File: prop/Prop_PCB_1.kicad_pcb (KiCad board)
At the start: 4 copper layers, 63.5 x 63.5 mm, 16 parts, among them J1 1984989, J2 1984989, J3 1984989, J4 1984989, J5 CAS_stacking, J6 Conn_01x02, J7 1984989, U1 L298P, U1301 MAX6675ISA+, U2 SN74LVC8T245DBR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

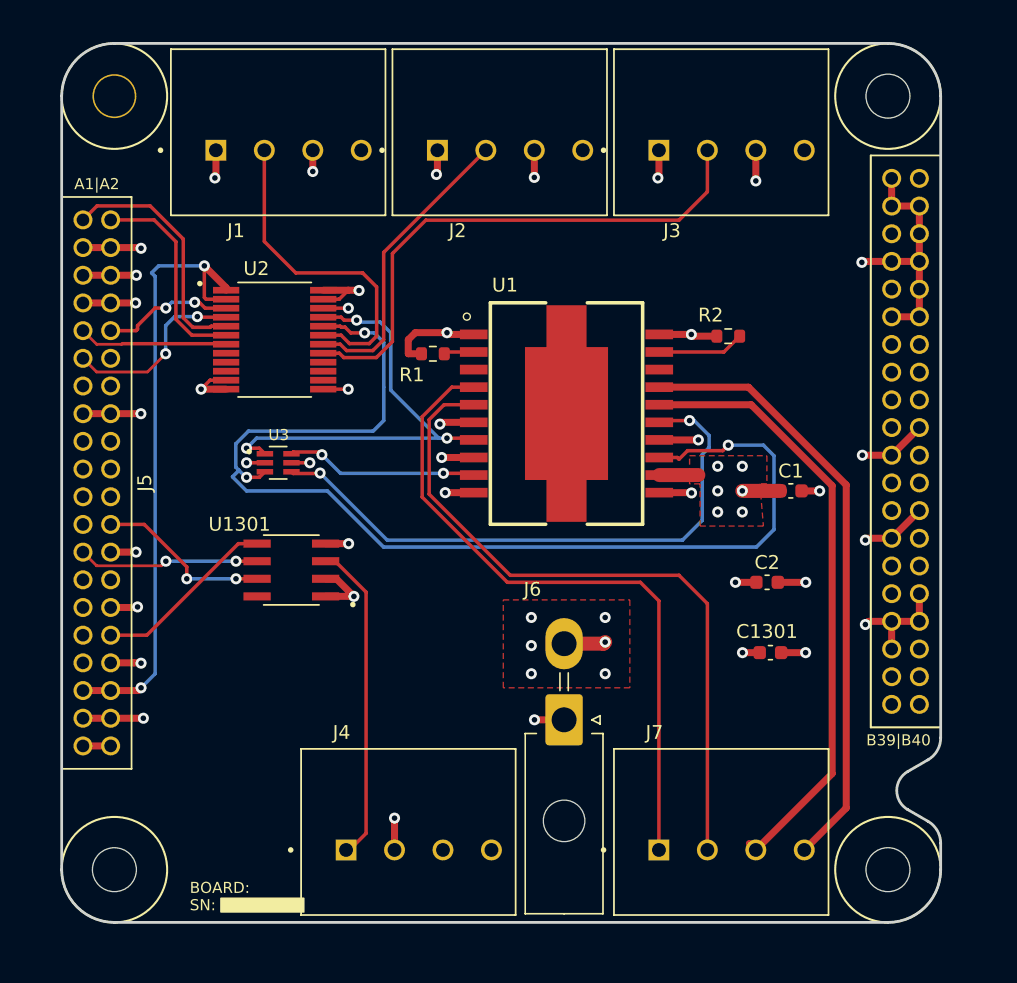
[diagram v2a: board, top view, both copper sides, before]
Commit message: Set minimum clearance to 0.25 mm.
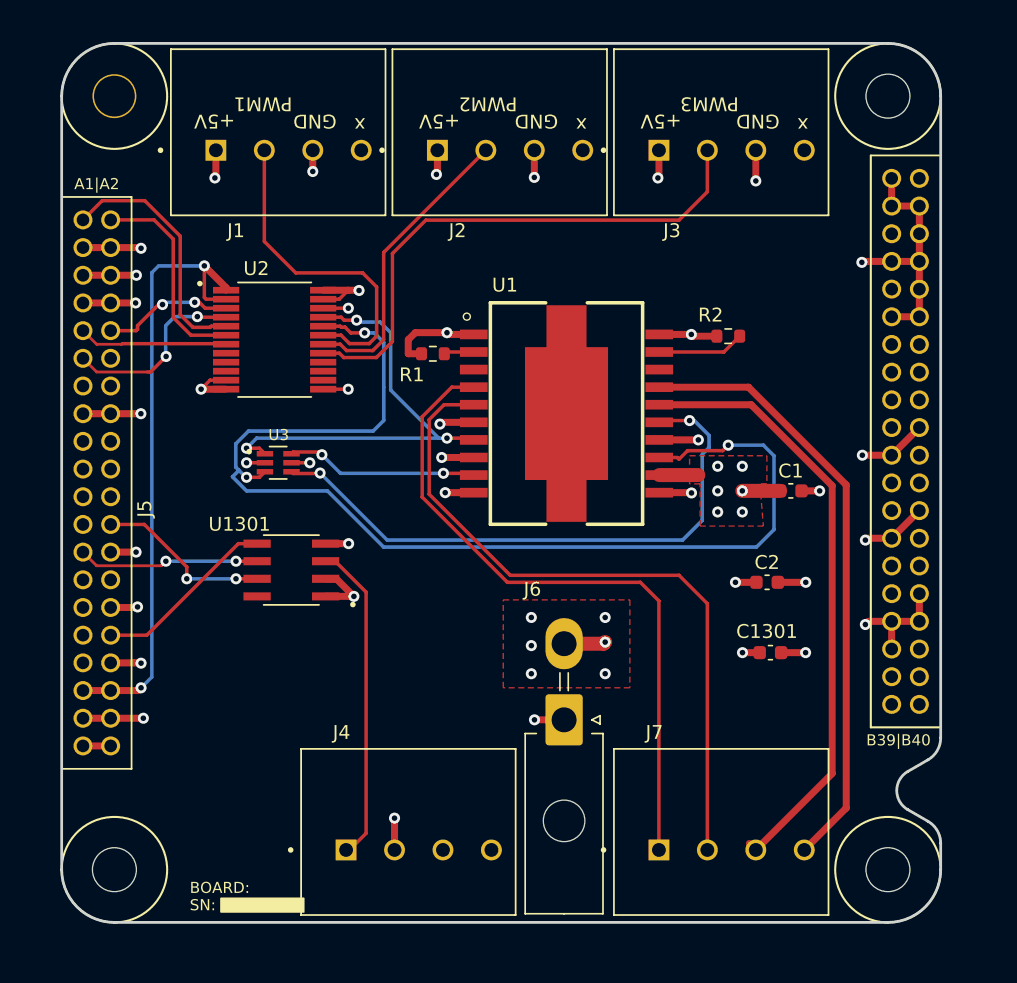
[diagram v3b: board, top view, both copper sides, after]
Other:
- board text added: "+5V"
- board text added: "GND"
- board text added: "PWM1"
- board text added: "PWM2"
- board text added: "PWM3"
- board text added: "x"
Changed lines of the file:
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@@
     (property "Sheetname" "CAS_bus")
     (attr through_hole)
-    (fp_text reference "J5" (at 6 31.75 90) (layer "F.SilkS")
+    (fp_text reference "J5" (at 6 33.615 90) (layer "F.SilkS")
       (effects (font (size 1 1) (thickness 0.15)))
     )
@@
       (effects (font (size 0.8 0.8) (thickness 0.15)))
     )
-    (fp_text user "ESQT-120-XX-XX-D" (at 57.277 35.767 270) (layer "F.Fab")
-      (effects (font (size 1 1) (thickness 0.015)))
-    )
-    (fp_text user "ESQT-120-XX-XX-D" (at 6.223 24.558 90) (layer "F.Fab")
+    (fp_text user "ESQT-120-XX-XX-D" (at 56.795 17.615 270) (layer "F.Fab")
       (effects (font (size 1 1) (thickness 0.015)))
     )
@@
     (pad "4" thru_hole circle locked (at 6 1.3) (size 1.508 1.508) (drill 1) (layers *.Cu *.Mask)
       (net 37 "unconnected-(J2-Pad4)") (pinfunction "4") (pintype "passive+no_connect"))
+  )
+  (gr_text "+5V" (at 97.25 50.25 180) (layer "F.SilkS")
+    (effects (font (size 1 1) (thickness 0.15)))
+  )
+  (gr_text "x" (at 91.5 50.5 180) (layer "F.SilkS")
+    (effects (font (size 1 1) (thickness 0.15)))
+  )
+  (gr_text "x" (at 107.5 50.5 180) (layer "F.SilkS")
+    (effects (font (size 1 1) (thickness 0.15)))
+  )
+  (gr_text "+5V" (at 81.25 50.25 180) (layer "F.SilkS")
+    (effects (font (size 1 1) (thickness 0.15)))
+  )
+  (gr_text "x" (at 75.5 50.5 180) (layer "F.SilkS")
+    (effects (font (size 1 1) (thickness 0.15)))
+  )
+  (gr_text "PWM2" (at 84.75 49 180) (layer "F.SilkS")
+    (effects (font (size 1 1) (thickness 0.15)))
+  )
+  (gr_text "+5V" (at 65 50.25 180) (layer "F.SilkS")
+    (effects (font (size 1 1) (thickness 0.15)))
+  )
+  (gr_text "GND" (at 88.25 50.25 180) (layer "F.SilkS")
+    (effects (font (size 1 1) (thickness 0.15)))
+  )
+  (gr_text "PWM3" (at 100.75 49 180) (layer "F.SilkS")
+    (effects (font (size 1 1) (thickness 0.15)))
+  )
+  (gr_text "GND" (at 104.25 50.25 180) (layer "F.SilkS")
+    (effects (font (size 1 1) (thickness 0.15)))
+  )
+  (gr_text "PWM1" (at 68.5 49 180) (layer "F.SilkS")
+    (effects (font (size 1 1) (thickness 0.15)))
+  )
+  (gr_text "GND" (at 72.25 50.25 180) (layer "F.SilkS")
+    (effects (font (size 1 1) (thickness 0.15)))
   )
   (segment (start 113.915 56.3851) (end 115.915 56.3851) (width 0.508) (layer "F.Cu") (net 1))
@@
   (via (at 64.262 60.706) (size 0.8) (drill 0.4) (layers "F.Cu" "B.Cu") (net 21))
   (via (at 59.69 91.186) (size 0.8) (drill 0.4) (layers "F.Cu" "B.Cu") (net 21))
-  (segment (start 60.706 61.468) (end 60.706 90.17) (width 0.254) (layer "B.Cu") (net 21))
-  (segment (start 60.706 90.17) (end 59.69 91.186) (width 0.254) (layer "B.Cu") (net 21))
-  (segment (start 60.96 60.706) (end 60.452 61.214) (width 0.254) (layer "B.Cu") (net 21))
-  (segment (start 60.452 61.214) (end 60.706 61.468) (width 0.254) (layer "B.Cu") (net 21))
+  (segment (start 60.464511 61.201489) (end 60.96 60.706) (width 0.25) (layer "B.Cu") (net 21))
+  (segment (start 59.69 91.186) (end 60.464511 90.411489) (width 0.25) (layer "B.Cu") (net 21))
+  (segment (start 60.464511 90.411489) (end 60.464511 61.201489) (width 0.25) (layer "B.Cu") (net 21))
   (segment (start 64.262 60.706) (end 60.96 60.706) (width 0.254) (layer "B.Cu") (net 21))
   (segment (start 64.322916 63.765) (end 63.905958 63.348042) (width 0.254) (layer "F.Cu") (net 22))
+  (segment (start 60.96 63.5) (end 60.706 63.754) (width 0.25) (layer "F.Cu") (net 22))
   (segment (start 59.436 65.278) (end 59.329 65.385) (width 0.254) (layer "F.Cu") (net 22))
   (segment (start 60.706 63.754) (end 59.436 65.024) (width 0.254) (layer "F.Cu") (net 22))
   (segment (start 63.905958 63.348042) (end 63.897177 63.339261) (width 0.254) (layer "F.Cu") (net 22))
-  (segment (start 61.4825 63.754) (end 60.706 63.754) (width 0.254) (layer "F.Cu") (net 22))
   (segment (start 59.436 65.024) (end 59.436 65.278) (width 0.254) (layer "F.Cu") (net 22))
   (segment (start 63.897177 63.339261) (end 63.567477 63.339261) (width 0.254) (layer "F.Cu") (net 22))
@@
   (segment (start 65.837 63.765) (end 65.833489 63.768511) (width 0.254) (layer "F.Cu") (net 22))
   (segment (start 59.329 65.385) (end 57.495 65.385) (width 0.254) (layer "F.Cu") (net 22))
+  (segment (start 61.239011 63.5) (end 60.96 63.5) (width 0.25) (layer "F.Cu") (net 22))
+  (via (at 61.239011 63.5) (size 0.8) (drill 0.4) (layers "F.Cu" "B.Cu") (net 22))
   (via (at 63.567477 63.339261) (size 0.8) (drill 0.4) (layers "F.Cu" "B.Cu") (net 22))
-  (via (at 61.4825 63.754) (size 0.8) (drill 0.4) (layers "F.Cu" "B.Cu") (net 22))
+  (segment (start 61.39975 63.339261) (end 61.239011 63.5) (width 0.25) (layer "B.Cu") (net 22))
   (segment (start 63.567477 63.339261) (end 61.897239 63.339261) (width 0.254) (layer "B.Cu") (net 22))
-  (segment (start 61.897239 63.339261) (end 61.4825 63.754) (width 0.254) (layer "B.Cu") (net 22))
+  (segment (start 61.897239 63.339261) (end 61.39975 63.339261) (width 0.25) (layer "B.Cu") (net 22))
+  (segment (start 60.378089 68.371911) (end 60.152089 68.371911) (width 0.254) (layer "F.Cu") (net 23))
   (segment (start 65.837 64.415) (end 65.803511 64.381511) (width 0.254) (layer "F.Cu") (net 23))
-  (segment (start 61.468 67.056) (end 60.152089 68.371911) (width 0.2032) (layer "F.Cu") (net 23))
+  (segment (start 61.5 67.25) (end 60.378089 68.371911) (width 0.254) (layer "F.Cu") (net 23))
   (segment (start 63.798841 64.415) (end 63.755605 64.371764) (width 0.254) (layer "F.Cu") (net 23))
   (segment (start 65.837 64.415) (end 63.798841 64.415) (width 0.254) (layer "F.Cu") (net 23))
   (segment (start 56.481911 68.371911) (end 55.495 67.385) (width 0.2032) (layer "F.Cu") (net 23))
   (segment (start 60.152089 68.371911) (end 56.481911 68.371911) (width 0.2032) (layer "F.Cu") (net 23))
+  (via (at 61.5 67.25) (size 0.8) (drill 0.4) (layers "F.Cu" "B.Cu") (net 23))
   (via (at 63.755605 64.371764) (size 0.8) (drill 0.4) (layers "F.Cu" "B.Cu") (net 23))
-  (via (at 61.468 67.056) (size 0.8) (drill 0.4) (layers "F.Cu" "B.Cu") (net 23))
   (segment (start 62.120236 64.371764) (end 61.468 65.024) (width 0.254) (layer "B.Cu") (net 23))
+  (segment (start 61.468 65.024) (end 61.468 67.218) (width 0.25) (layer "B.Cu") (net 23))
+  (segment (start 61.468 67.218) (end 61.5 67.25) (width 0.25) (layer "B.Cu") (net 23))
   (segment (start 63.755605 64.371764) (end 62.120236 64.371764) (width 0.254) (layer "B.Cu") (net 23))
-  (segment (start 61.468 65.024) (end 61.468 67.056) (width 0.254) (layer "B.Cu") (net 23))
   (segment (start 65.837 65.065) (end 64.763557 65.065) (width 0.254) (layer "F.Cu") (net 24))
+  (segment (start 62.519041 58.556957) (end 59.962084 56) (width 0.254) (layer "F.Cu") (net 24))
   (segment (start 64.763557 65.065) (end 64.680282 65.148275) (width 0.254) (layer "F.Cu") (net 24))
-  (segment (start 62.738 58.762) (end 60.348689 56.372689) (width 0.254) (layer "F.Cu") (net 24))
-  (segment (start 60.348689 56.372689) (end 56.507311 56.372689) (width 0.254) (layer "F.Cu") (net 24))
-  (segment (start 56.507311 56.372689) (end 55.495 57.385) (width 0.254) (layer "F.Cu") (net 24))
+  (segment (start 56.88 56) (end 55.495 57.385) (width 0.254) (layer "F.Cu") (net 24))
+  (segment (start 62.519042 64.233354) (end 62.519041 58.556957) (width 0.254) (layer "F.Cu") (net 24))
   (segment (start 64.680282 65.148275) (end 63.433963 65.148275) (width 0.254) (layer "F.Cu") (net 24))
-  (segment (start 63.433963 65.148275) (end 62.738 64.452312) (width 0.254) (layer "F.Cu") (net 24))
-  (segment (start 62.738 64.452312) (end 62.738 58.762) (width 0.254) (layer "F.Cu") (net 24))
+  (segment (start 59.962084 56) (end 56.88 56) (width 0.254) (layer "F.Cu") (net 24))
+  (segment (start 63.433963 65.148275) (end 62.519042 64.233354) (width 0.254) (layer "F.Cu") (net 24))
+  (segment (start 65.837 65.715) (end 63.288604 65.715) (width 0.254) (layer "F.Cu") (net 25))
+  (segment (start 62.015522 58.765522) (end 60.635 57.385) (width 0.254) (layer "F.Cu") (net 25))
   (segment (start 60.635 57.385) (end 57.495 57.385) (width 0.254) (layer "F.Cu") (net 25))
-  (segment (start 65.837 65.715) (end 63.359314 65.715) (width 0.254) (layer "F.Cu") (net 25))
-  (segment (start 62.209011 64.564697) (end 62.209011 58.959011) (width 0.254) (layer "F.Cu") (net 25))
-  (segment (start 62.209011 58.959011) (end 60.635 57.385) (width 0.254) (layer "F.Cu") (net 25))
-  (segment (start 63.359314 65.715) (end 62.209011 64.564697) (width 0.254) (layer "F.Cu") (net 25))
+  (segment (start 63.288604 65.715) (end 62.015522 64.441918) (width 0.254) (layer "F.Cu") (net 25))
+  (segment (start 62.015522 64.441918) (end 62.015522 58.765522) (width 0.254) (layer "F.Cu") (net 25))
   (segment (start 65.801489 66.329489) (end 58.329489 66.329489) (width 0.254) (layer "F.Cu") (net 26))
   (segment (start 58.329489 66.329489) (end 58.287067 66.371911) (width 0.2032) (layer "F.Cu") (net 26))
   (segment (start 56.481911 66.371911) (end 55.495 65.385) (width 0.2032) (layer "F.Cu") (net 26))
-  (segment (start 65.837 66.365) (end 65.801489 66.329489) (width 0.254) (layer "F.Cu") (net 26))
   (segment (start 58.287067 66.371911) (end 56.481911 66.371911) (width 0.2032) (layer "F.Cu") (net 26))
   (segment (start 77.849042 66.168958) (end 77.849042 59.815042) (width 0.254) (layer "F.Cu") (net 33))

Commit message: Updated hard-sch-blocks
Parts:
- moved C1301 24.7 mm to (80.5, 89.2)
- moved C2 24.7 mm to (80.3, 84.2)
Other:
- board text added: "Lead1"
- board text added: "Lead2"
- board text added: "Sol1"
- board text added: "Sol2"
- board text added: "T+"

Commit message: Added Star, BAC logo.
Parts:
- added Ref**: Val**, star-common-lib:star_fancy, F.Cu at (66.0, 91.0)
- added Ref**: Val**, star-common-lib:bac, F.Cu at (66.5, 98.8)

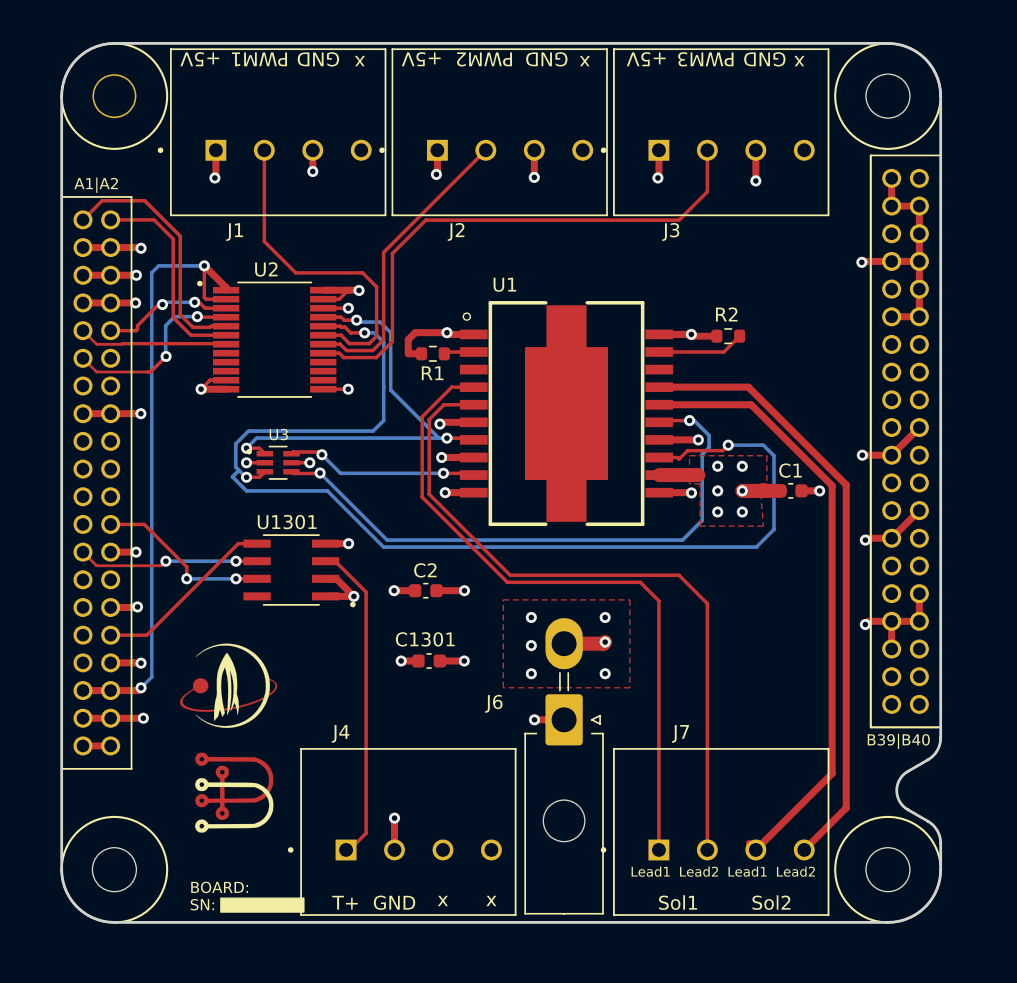
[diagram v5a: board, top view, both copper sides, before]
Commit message: Added front/back ground pour.
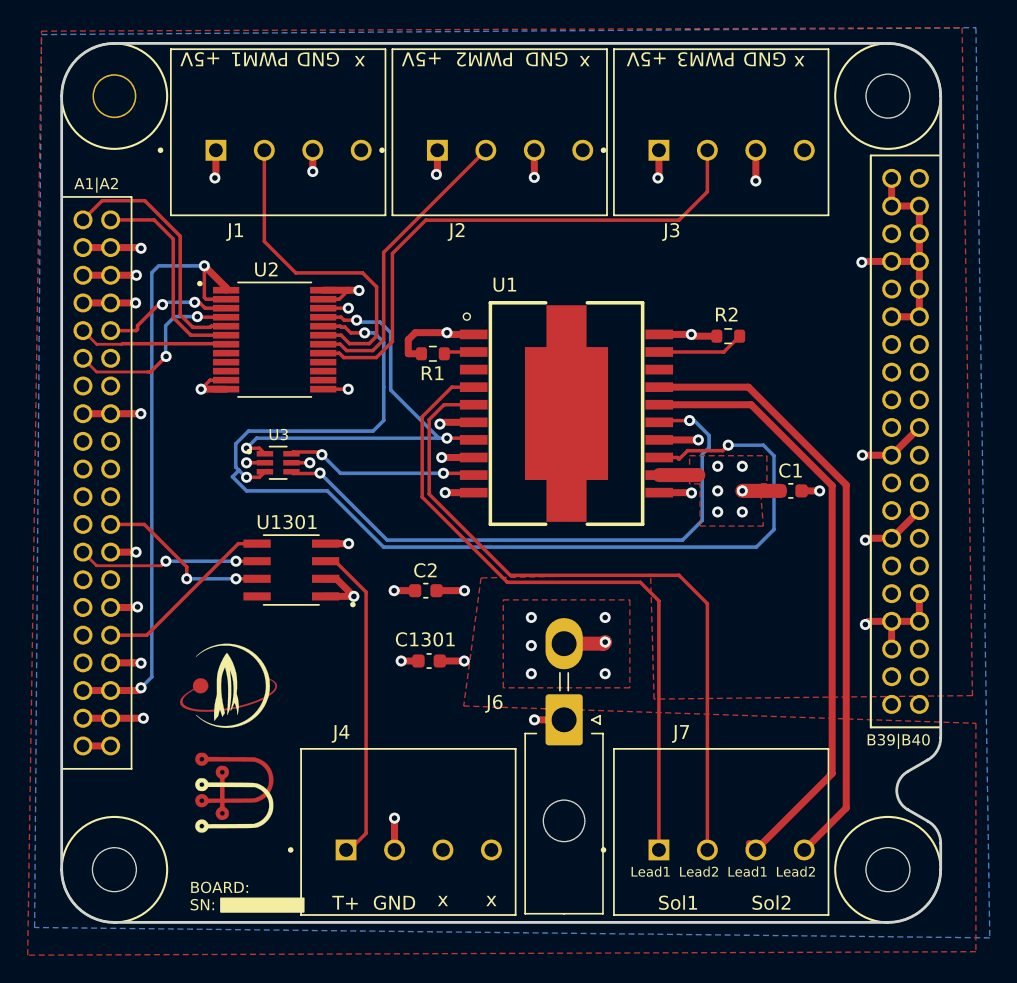
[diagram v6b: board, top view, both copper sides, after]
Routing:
- added copper zone on B.Cu, net GND
- added copper zone on F.Cu, net GND
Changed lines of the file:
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@@
   (segment (start 70.866 61.214) (end 68.596 58.944) (width 0.254) (layer "F.Cu") (net 35))
   (segment (start 57.495 95.3849) (end 55.495 95.3849) (width 0.508) (layer "F.Cu") (net 42))
+  (zone (net 1) (net_name "GND") (layer "F.Cu") (hatch edge 0.508)
+    (connect_pads (clearance 0.508))
+    (min_thickness 0.254) (filled_areas_thickness no)
+    (fill yes (thermal_gap 0.508) (thermal_bridge_width 0.508))
+    (polygon
+      (pts
+        (xy 119.75 91.75)
+        (xy 96.75 92)
+        (xy 96.5 83)
+        (xy 84.25 83.25)
+        (xy 83 92.5)
+        (xy 120 93.75)
+        (xy 120 110.25)
+        (xy 51.5 110.5)
+        (xy 52.5 43.75)
+        (xy 119 43.5)
+      )
+    )
+  )
   (zone (net 14) (net_name "+24V") (layer "F.Cu") (hatch edge 0.508)
     (connect_pads (clearance 0.508))
@@
       )
     )
+  )
+  (zone (net 1) (net_name "GND") (layer "B.Cu") (hatch edge 0.508)
+    (connect_pads (clearance 0.508))
+    (min_thickness 0.254) (filled_areas_thickness no)
+    (fill yes (thermal_gap 0.508) (thermal_bridge_width 0.508))
+    (polygon
+      (pts
+        (xy 121 109.25)
+        (xy 52 108.5)
+        (xy 52.5 44)
+        (xy 120 43.5)
+      )
+    )
